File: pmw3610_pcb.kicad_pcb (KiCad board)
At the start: 2 copper layers, 23.5 x 31.5 mm, 24 parts, among them J1 Conn_PinHeader, J2 Conn_FPC, U1 PMW3610, U2 TLV74318PDBVR

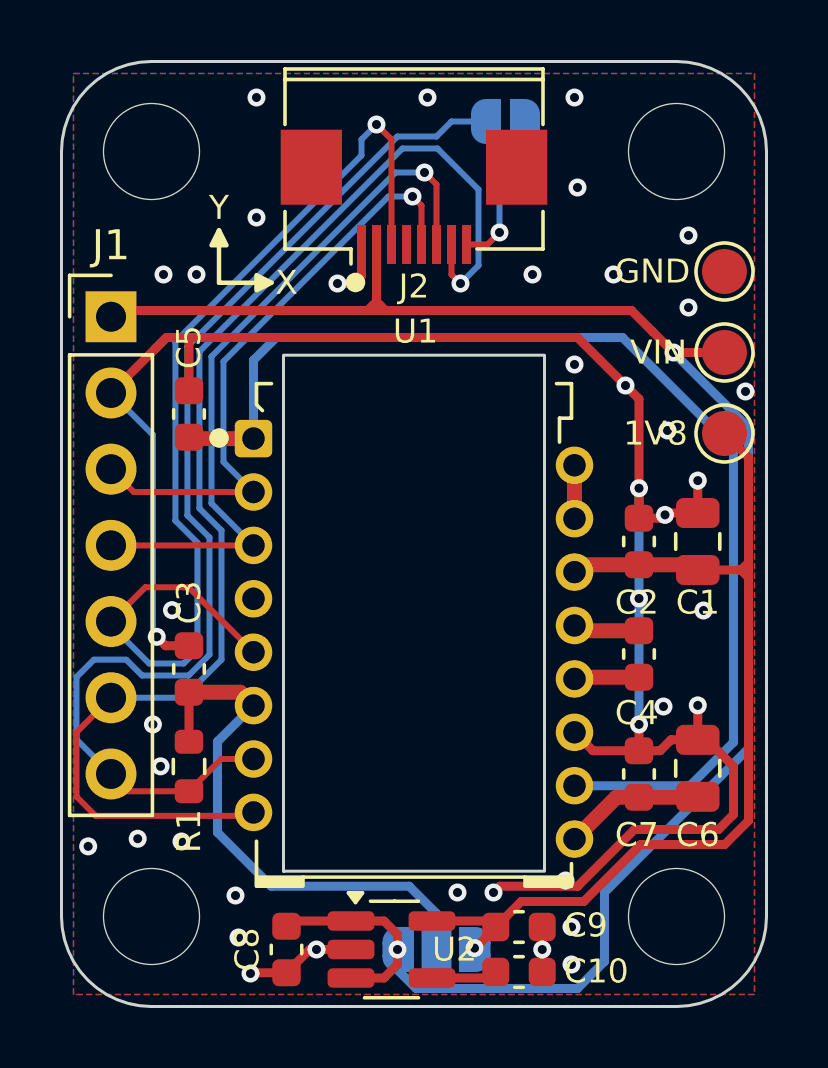
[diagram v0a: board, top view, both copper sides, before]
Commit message: feat: add top silkscreen header labels and reroute traces
What this commit
  contains:

  - Adds readable top-side header labels for J1 for soldering.
  - Updates board/schematic revision to 2.2.
  - Reroutes traces and nearby items to fit the silkscreen labels.
  - Swaps TP1/TP2 placement intentionally for routing, with schematic and PCB matching.
  - Includes the KiCad 10 project update in .kicad_pro.
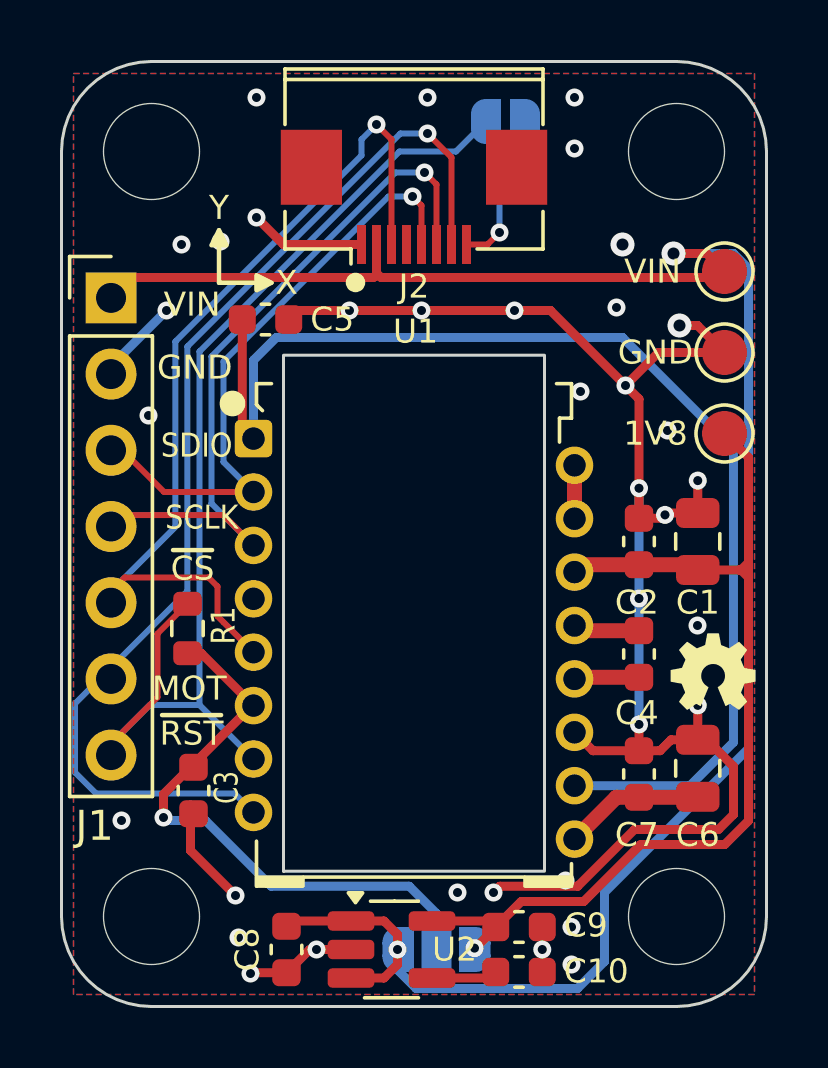
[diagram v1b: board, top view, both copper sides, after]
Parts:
- moved R1 4.60 mm to (142.4, 103.2), turned to 90 degrees
- moved C5 4.05 mm to (145.1, 92.8), turned to 0 degrees
- moved C3 4.05 mm to (142.7, 108.5), turned to -90 degrees
- moved J1 0.63 mm to (139.9, 92.1)
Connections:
- TP1 pad 1: GND -> VIN
- TP2 pad 1: VIN -> GND
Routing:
- net VIN: track 62.5 -> 67.4 mm
- net MOTION: track 42.3 -> 37.4 mm
- net nCS: track 34.6 -> 30.0 mm
- net GND: track 70.5 -> 66.4 mm, vias 41 -> 36
- net Net-(U1-+VCSEL): track 38.3 -> 40.5 mm
- net nRESET: track 38.0 -> 36.3 mm
- net VDDIO: track 18.3 -> 19.9 mm, vias 0 -> 1

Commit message: fix: correct assembly metadata and FPC footprint origin
What this commit
  contains:

  - Excludes J1 from PCB assembly BOM/position outputs so JLC does not place the header.
  - Excludes C10 from BOM/position outputs while leaving it DNP.
  - Corrects the J2 FPC footprint origin so JLC placement previews correctly.
  - Updates the local FPC footprint library and placed footprint to match.
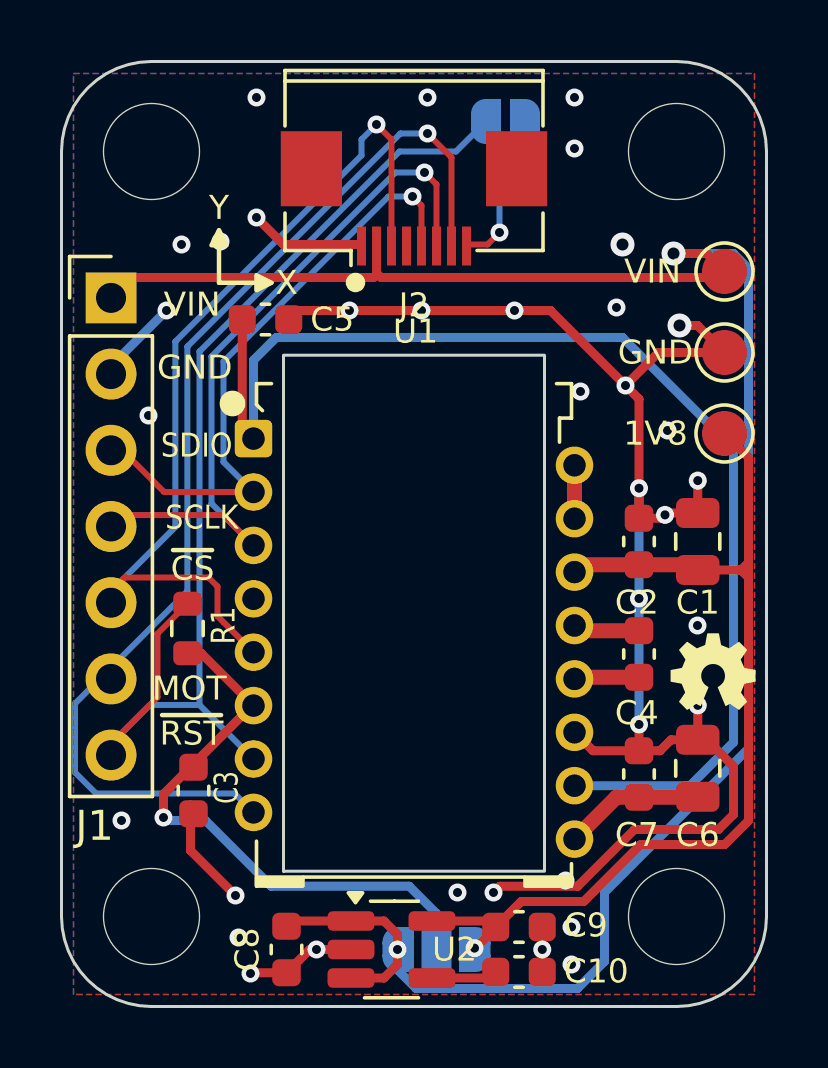
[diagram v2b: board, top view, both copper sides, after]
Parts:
- moved J2 1.55 mm to (150.0, 88.9)
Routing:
- net VIN: track 67.4 -> 66.4 mm
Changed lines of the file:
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@@
 		(sheetname "/")
 		(sheetfile "pmw3610_pcb.kicad_sch")
-		(attr smd dnp)
+		(attr smd exclude_from_pos_files exclude_from_bom dnp)
 		(duplicate_pad_numbers_are_jumpers no)
 		(fp_line
@@
 	(footprint "pmw3610_pcb:FPC_8P_0.5mm_AFC01-S08FCA-00"
 		(layer "F.Cu")
-		(at 150 87.35)
+		(at 150 88.9)
 		(descr "AFC01-S08FCA-00")
-		(property "Reference" "J2"
-			(at 0 4.4 0)
-			(unlocked yes)
-			(layer "F.SilkS")
-			(effects
-				(font
-					(size 0.8 0.8)
-					(thickness 0.15)
-				)
-			)
-		)
-		(property "Value" "Conn_FPC"
-			(at 0 0.5 0)
-			(unlocked yes)
-			(layer "F.Fab")
-			(effects
-				(font
-					(size 1 1)
-					(thickness 0.15)
-				)
-			)
-		)
 		(property "Datasheet" ""
 			(at 0 0 0)
@@
 			)
 		)
+		(property "Value" "Conn_FPC"
+			(at 0 -0.425 0)
+			(unlocked yes)
+			(layer "F.Fab")
+			(effects
+				(font
+					(size 1 1)
+					(thickness 0.15)
+				)
+			)
+		)
+		(property "Reference" "J2"
+			(at 0 3.475 0)
+			(unlocked yes)
+			(layer "F.SilkS")
+			(effects
+				(font
+					(size 0.8 0.8)
+					(thickness 0.15)
+				)
+			)
+		)
 		(property "JLCPCB Part #" "C262657"
 			(at 0 0 180)
@@
 		(duplicate_pad_numbers_are_jumpers no)
 		(fp_line
-			(start -4.3 -2.85)
-			(end -4.3 -1)
+			(start -4.3 -4.35)
+			(end -4.3 -2.5)
 			(stroke
 				(width 0.12)
@@
 		)
 		(fp_line
-			(start -4.3 -2.85)
-			(end 4.3 -2.85)
+			(start -4.3 -4.35)
+			(end 4.3 -4.35)
 			(stroke
 				(width 0.12)
@@
 		)
 		(fp_line
-			(start -4.3 1.9)
-			(end -4.3 3.15)
+			(start -4.3 0.4)
+			(end -4.3 1.65)
 			(stroke
 				(width 0.12)
@@
 		)
 		(fp_line
-			(start -4.3 3.15)
-			(end -2.1 3.15)
+			(start -4.3 1.65)
+			(end -2.1 1.65)
 			(stroke
 				(width 0.12)
@@
 		)
 		(fp_line
-			(start -2.1 3.15)
-			(end -2.1 3.65)
+			(start -2.1 1.65)
+			(end -2.1 2.15)
 			(stroke
 				(width 0.12)
@@
 		)
 		(fp_line
-			(start 4.3 -2.85)
-			(end 4.3 -1)
+			(start 4.3 -4.35)
+			(end 4.3 -2.5)
 			(stroke
 				(width 0.12)
@@
 		)
 		(fp_line
-			(start 4.3 -2.5)
-			(end -4.3 -2.5)
+			(start 4.3 -4)
+			(end -4.3 -4)
 			(stroke
 				(width 0.12)
@@
 		)
 		(fp_line
-			(start 4.3 1.9)
-			(end 4.3 3.15)
+			(start 4.3 0.4)
+			(end 4.3 1.65)
 			(stroke
 				(width 0.12)
@@
 		)
 		(fp_line
-			(start 4.3 3.15)
-			(end 2.1 3.15)
+			(start 4.3 1.65)
+			(end 2.1 1.65)
 			(stroke
 				(width 0.12)
@@
 		)
 		(fp_rect
-			(start -4.75 -3.5)
-			(end 4.75 4)
+			(start -4.75 -5)
+			(end 4.75 2.5)
 			(stroke
 				(width 0.05)
@@
 		)
 		(fp_text user "${REFERENCE}"
-			(at 0 4.5 0)
+			(at 0 3.575 0)
 			(unlocked yes)
 			(layer "F.Fab")
@@
 		)
 		(pad "1" smd rect
-			(at -1.75 3)
+			(at -1.75 1.5)
 			(size 0.3 1.3)
 			(layers "F.Cu" "F.Mask" "F.Paste")
@@
 		)
 		(pad "2" smd rect
-			(at -1.25 3)
+			(at -1.25 1.5)
 			(size 0.3 1.3)
 			(layers "F.Cu" "F.Mask" "F.Paste")
@@
 		)
 		(pad "3" smd rect
-			(at -0.75 3)
+			(at -0.75 1.5)
 			(size 0.3 1.3)
 			(layers "F.Cu" "F.Mask" "F.Paste")
@@
 		)
 		(pad "4" smd rect
-			(at -0.25 3)
+			(at -0.25 1.5)
 			(size 0.3 1.3)
 			(layers "F.Cu" "F.Mask" "F.Paste")
@@
 		)
 		(pad "5" smd rect
-			(at 0.25 3)
+			(at 0.25 1.5)
 			(size 0.3 1.3)
 			(layers "F.Cu" "F.Mask" "F.Paste")
@@
 		)
 		(pad "6" smd rect
-			(at 0.75 3)
+			(at 0.75 1.5)
 			(size 0.3 1.3)
 			(layers "F.Cu" "F.Mask" "F.Paste")
@@
 		)
 		(pad "7" smd rect
-			(at 1.25 3)
+			(at 1.25 1.5)
 			(size 0.3 1.3)
 			(layers "F.Cu" "F.Mask" "F.Paste")
@@
 		)
 		(pad "8" smd rect
-			(at 1.75 3)
+			(at 1.75 1.5)
 			(size 0.3 1.3)
 			(layers "F.Cu" "F.Mask" "F.Paste")
@@
 		)
 		(pad "MP" smd rect
-			(at -3.42 0.425)
+			(at -3.42 -1.075)
 			(size 2.04 2.5)
 			(layers "F.Cu" "F.Mask" "F.Paste")
@@
 		)
 		(pad "MP" smd rect
-			(at 3.42 0.425)
+			(at 3.42 -1.075)
 			(size 2.04 2.5)
 			(layers "F.Cu" "F.Mask" "F.Paste")
@@
 		(sheetname "/")
 		(sheetfile "pmw3610_pcb.kicad_sch")
-		(attr through_hole)
+		(attr through_hole exclude_from_pos_files exclude_from_bom dnp)
 		(duplicate_pad_numbers_are_jumpers no)
 		(fp_line
@@
 		(width 0.3)
 		(layer "F.Cu")
-		(net "VIN")
-	)
-	(segment
-		(start 148.75 90.35)
-		(end 148.75 91.3)
-		(width 0.3)
-		(layer "F.Cu")
